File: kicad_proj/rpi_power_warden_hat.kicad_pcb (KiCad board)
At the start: 4 copper layers, 65 x 56.5 mm, 67 parts, among them J1 54-00164, J2 54-00164, J3 54-00003, J4 Raspberry Pi SMT connector, J5 Conn_01x02, Q1 DMG2305UX-7, Q2 DMG2305UX-7, U1 INA260, U10 SN74AHC1G08DBVR, U2 INA260, U3 CAT24C32WI-GT3, U4 TPS563200, U5 DMMT5401-7-F, U6 TPS563200, U7 DMMT5401-7-F, U8 TPS22810DBVR, U9 SN74AHC1G08DBVR

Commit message: progress with layout
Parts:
- moved C17 4.25 mm to (154.5, 82.9), turned to 0 degrees
- moved U10 1.32 mm to (154.1, 85.5)
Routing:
- added copper zone on F.Cu, net /current_sensor_5V/+VCC_OUT
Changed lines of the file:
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@@
 	(footprint "rpi_power_warden_hat:SOT-23-5"
 		(layer "F.Cu")
-		(at 153.5653 86.672448)
+		(at 154.088679 85.458721)
 		(descr "SOT, 5 Pin (JEDEC MO-178 Var AA https://www.jedec.org/document_search?search_api_views_fulltext=MO-178), generated with kicad-footprint-generator ipc_gullwing_generator.py")
 		(tags "SOT TO_SOT_SMD")
 		(property "Reference" "U10"
-			(at 0 -2.61 0)
+			(at 0 2.3368 0)
 			(layer "F.SilkS")
 			(effects
@@
 	(footprint "Capacitor_SMD:C_0603_1608Metric_Pad1.08x0.95mm_HandSolder"
 		(layer "F.Cu")
-		(at 156.561479 86.622448 90)
+		(at 154.459658 82.924194)
 		(descr "Capacitor SMD 0603 (1608 Metric), square (rectangular) end terminal, IPC_7351 nominal with elongated pad for handsoldering. (Body size source: IPC-SM-782 page 76, https://www.pcb-3d.com/wordpress/wp-content/uploads/ipc-sm-782a_amendment_1_and_2.pdf), generated with kicad-footprint-generator")
 		(tags "capacitor handsolder")
 		(property "Reference" "C17"
-			(at 0.011327 1.515 90)
+			(at 0.011327 -1.224673 360)
 			(layer "F.SilkS")
 			(effects
@@
 		)
 		(property "Value" "100 nF"
-			(at 0 1.43 90)
+			(at 0 1.43 360)
 			(layer "F.Fab")
 			(effects
@@
 		)
 		(property "Footprint" "Capacitor_SMD:C_0603_1608Metric_Pad1.08x0.95mm_HandSolder"
-			(at 0 0 90)
+			(at 0 0 0)
 			(unlocked yes)
 			(layer "F.Fab")
@@
 		)
 		(property "Datasheet" ""
-			(at 0 0 90)
+			(at 0 0 0)
 			(unlocked yes)
 			(layer "F.Fab")
@@
 		)
 		(property "Description" "CAP 0603 25V 100 NF X5R"
-			(at 0 0 90)
+			(at 0 0 0)
 			(unlocked yes)
 			(layer "F.Fab")
@@
 		)
 		(property "mpn" "CC0603KRX5R8BB104"
-			(at 0 0 90)
+			(at 0 0 0)
 			(unlocked yes)
 			(layer "F.Fab")
@@
 		)
 		(property "manufacturer" "YAGEO"
-			(at 0 0 90)
+			(at 0 0 0)
 			(unlocked yes)
 			(layer "F.Fab")
@@
 		)
 		(fp_line
-			(start 1.65 -0.73)
-			(end 1.65 0.73)
+			(start -1.65 -0.73)
+			(end 1.65 -0.73)
 			(stroke
 				(width 0.05)
@@
 		)
 		(fp_line
-			(start -1.65 -0.73)
-			(end 1.65 -0.73)
+			(start -1.65 0.73)
+			(end -1.65 -0.73)
 			(stroke
 				(width 0.05)
@@
 		)
 		(fp_line
-			(start 1.65 0.73)
-			(end -1.65 0.73)
+			(start 1.65 -0.73)
+			(end 1.65 0.73)
 			(stroke
 				(width 0.05)
@@
 		)
 		(fp_line
-			(start -1.65 0.73)
-			(end -1.65 -0.73)
+			(start 1.65 0.73)
+			(end -1.65 0.73)
 			(stroke
 				(width 0.05)
@@
 		)
 		(fp_line
-			(start 0.8 -0.4)
-			(end 0.8 0.4)
+			(start -0.8 -0.4)
+			(end 0.8 -0.4)
 			(stroke
 				(width 0.1)
@@
 		)
 		(fp_line
-			(start -0.8 -0.4)
-			(end 0.8 -0.4)
+			(start -0.8 0.4)
+			(end -0.8 -0.4)
 			(stroke
 				(width 0.1)
@@
 		)
 		(fp_line
-			(start 0.8 0.4)
-			(end -0.8 0.4)
+			(start 0.8 -0.4)
+			(end 0.8 0.4)
 			(stroke
 				(width 0.1)
@@
 		)
 		(fp_line
-			(start -0.8 0.4)
-			(end -0.8 -0.4)
+			(start 0.8 0.4)
+			(end -0.8 0.4)
 			(stroke
 				(width 0.1)
@@
 		)
 		(fp_text user "${REFERENCE}"
-			(at 0 0 90)
+			(at 0 0 360)
 			(layer "F.Fab")
 			(effects
@@
 		)
 		(pad "1" smd roundrect
-			(at -0.8625 0 90)
+			(at -0.8625 0)
 			(size 1.075 0.95)
 			(layers "F.Cu" "F.Paste" "F.Mask")
@@
 		)
 		(pad "2" smd roundrect
-			(at 0.8625 0 90)
+			(at 0.8625 0)
 			(size 1.075 0.95)
 			(layers "F.Cu" "F.Paste" "F.Mask")
@@
 	)
 	(gr_rect
-		(start 151.379479 83.335169)
+		(start 151.379479 80.957321)
 		(end 158.745479 88.501121)
 		(stroke
@@
 	)
 	(segment
-		(start 160.311059 105.8892)
-		(end 160.311059 104.0781)
-		(width 0.5)
+		(start 160.311059 104.0781)
+		(end 160.416759 103.9724)
+		(width 0.254)
 		(layer "F.Cu")
 		(net 3)
 	)
 	(segment
-		(start 160.311059 104.0781)
-		(end 160.416759 103.9724)
-		(width 0.254)
+		(start 160.641879 105.973071)
+		(end 160.641879 104.161971)
+		(width 0.5)
 		(layer "F.Cu")
 		(net 3)
@@
 	(segment
 		(start 168.973079 104.559521)
-		(end 169.074679 104.661121)
-		(width 0.254)
-		(layer "F.Cu")
-		(net 6)
-	)
-	(segment
-		(start 166.382279 104.559521)
-		(end 168.973079 104.559521)
+		(end 166.382279 104.559521)
 		(width 0.254)
 		(layer "F.Cu")
@@
 	)
 	(via
-		(at 169.074679 104.661121)
+		(at 168.973079 104.559521)
 		(size 0.45)
 		(drill 0.15)
@@
 	)
 	(segment
-		(start 169.074679 104.661121)
-		(end 169.074679 100.327321)
+		(start 168.973079 104.559521)
+		(end 168.973079 100.225721)
 		(width 0.254)
 		(layer "B.Cu")
@@
 	)
 	(segment
-		(start 169.074679 100.327321)
+		(start 168.973079 100.225721)
 		(end 164.299479 95.552121)
 		(width 0.254)
@@
 	)
 	(segment
-		(start 154.7028 87.622448)
-		(end 154.7028 88.4006)
-		(width 0.254)
-		(layer "F.Cu")
-		(net 71)
-	)
-	(segment
-		(start 154.7028 88.4006)
-		(end 154.698279 88.405121)
+		(start 155.226179 86.408721)
+		(end 155.226179 87.877221)
 		(width 0.254)
 		(layer "F.Cu")
@@
 	)
 	(via
-		(at 154.698279 88.455921)
+		(at 155.226179 87.877221)
 		(size 0.45)
 		(drill 0.15)
@@
 	)
 	(segment
-		(start 156.222279 88.455921)
-		(end 154.698279 88.455921)
+		(start 155.643579 87.877221)
+		(end 168.058679 100.292321)
 		(width 0.254)
 		(layer "B.Cu")
@@
 	(segment
 		(start 168.058679 100.292321)
-		(end 156.222279 88.455921)
+		(end 168.058679 102.933921)
 		(width 0.254)
 		(layer "B.Cu")
@@
 	)
 	(segment
-		(start 168.058679 102.933921)
-		(end 168.058679 100.292321)
+		(start 155.226179 87.877221)
+		(end 155.643579 87.877221)
 		(width 0.254)
 		(layer "B.Cu")
@@
 			(thermal_gap 0.25)
 			(thermal_bridge_width 0.5)
+			(smoothing chamfer)
+			(radius 0.15)
 		)
 		(polygon
 			(pts
 				(xy 160.489479 91.554721) (xy 160.489479 93.617824) (xy 153.674352 93.614854) (xy 153.680891 89.065521)
-				(xy 157.746279 89.065521) (xy 157.746279 90.945121) (xy 162.521479 90.945121) (xy 163.131079 91.554721)
+				(xy 156.641263 89.065521) (xy 156.621654 82.102972) (xy 163.334279 82.108235) (xy 163.334279 84.645921)
+				(xy 158.408358 84.645921) (xy 158.406679 89.064905) (xy 160.895879 89.065695) (xy 163.364726 91.554721)
 			)
 		)
@@
 			)
 		)
+	)
+	(zone
+		(net 15)
+		(net_name "/current_sensor_5V/+VCC_OUT")
+		(layer "F.Cu")
+		(hatch edge 0.5)
+		(priority 2)
+		(connect_pads
+			(clearance 0.25)
+		)
+		(min_thickness 0.25)
+		(filled_areas_thickness no)
+		(fill yes
+			(thermal_gap 0.25)
+			(thermal_bridge_width 0.5)
+			(smoothing chamfer)
+			(radius 0.15)
+		)
+		(polygon
+			(pts
+				(xy 165.772679 84.645921) (xy 172.173479 84.645921) (xy 172.173479 84.645921) (xy 172.173479 93.434321)
+				(xy 172.173479 93.434321) (xy 179.082279 93.434321) (xy 179.133079 93.383521) (xy 179.133079 90.843521)
+				(xy 179.082279 90.792721) (xy 174.662679 90.792721) (xy 174.662679 90.792721) (xy 174.662679 82.055121)
+				(xy 174.662679 82.055121) (xy 165.772679 82.055121)
+			)
+		)

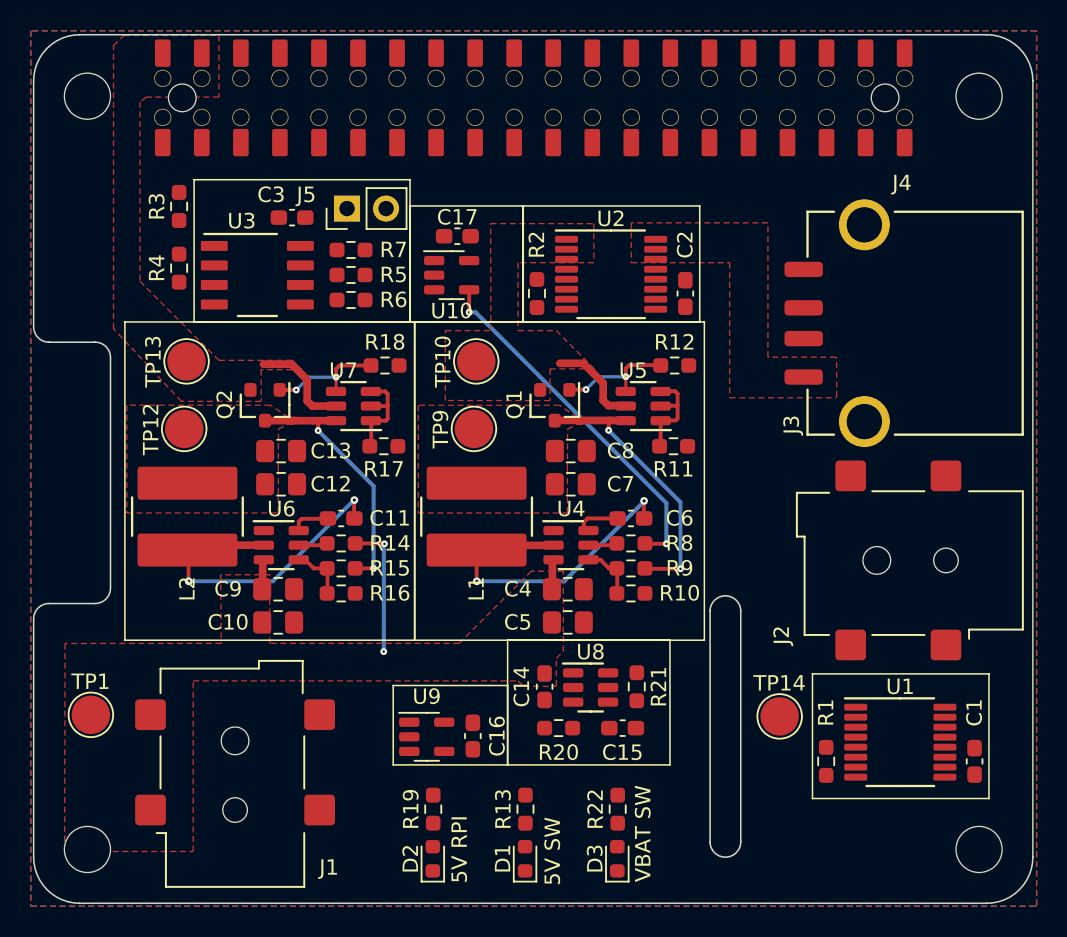
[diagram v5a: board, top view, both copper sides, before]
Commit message: feat: replace tht jumper by as solder bridge. feat: progress with layout.
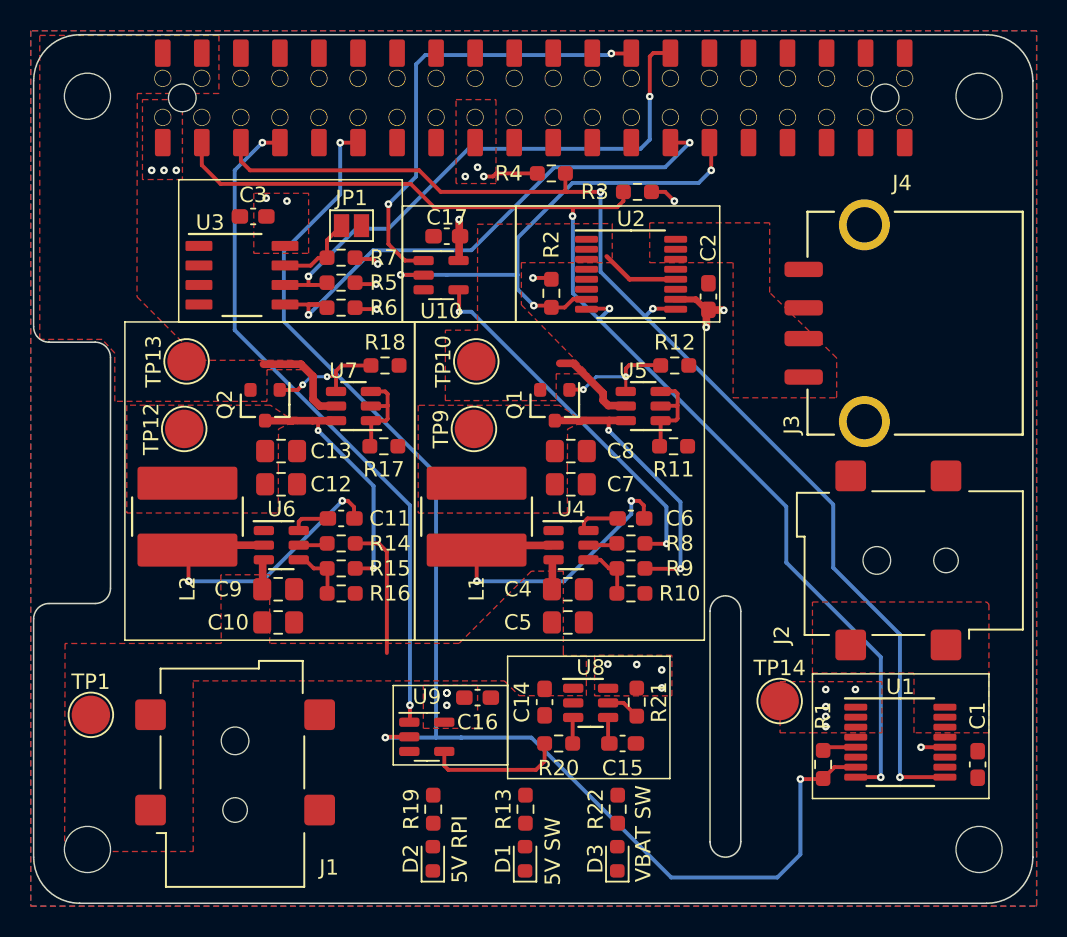
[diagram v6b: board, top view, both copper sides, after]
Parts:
- removed J5: Conn_01x02, Connector_PinHeader_2.54mm:PinHeader_1x02_P2.54mm_Vertical
- added JP1: SolderJumper_2_Open, Jumper:SolderJumper-2_P1.3mm_Open_Pad1.0x1.5mm, F.Cu at (147.6, 82.2)
- moved R3 29.8 mm to (166.2, 80.0), turned to 180 degrees
- moved R4 25.0 mm to (160.6, 78.8), turned to 0 degrees
- moved C3 2.54 mm to (141.2, 81.6)
- moved C16 2.52 mm to (155.8, 112.9), turned to 180 degrees
- moved C2 1.51 mm to (170.8, 86.8)
- moved U2 1.30 mm to (165.8, 85.4)
- moved C14 1.00 mm to (160.1, 113.2)
- moved C15 1.00 mm to (165.2, 115.9)
- moved R20 1.00 mm to (161.0, 115.9)
- moved R21 1.00 mm to (166.1, 113.2)
- moved TP14 1.00 mm to (175.4, 113.2)
- moved U3 1.00 mm to (140.4, 85.4)
- moved U8 1.00 mm to (163.1, 113.3)
- moved R2 0.94 mm to (160.6, 86.6), turned to 90 degrees
- moved R5 0.82 mm to (146.9, 85.9)
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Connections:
- J4 pad 26: /rpi/ENA_VBAT_SW -> /rpi/ENA_5V_SW
- J4 pad 29: /rpi/ENA_5V_SW -> /rpi/INA_5V_ALERT
- J4 pad 7: /rpi/INA_5V_ALERT -> /rpi/ENA_VBAT_SW
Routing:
- net /rpi/INA_VBAT_ALERT: track 0.00 -> 87.3 mm, vias 0 -> 3
- net /INA_SDA: track 0.00 -> 80.3 mm, vias 0 -> 3
- net /INA_SCL: track 0.00 -> 77.6 mm, vias 0 -> 3
- net /rpi/ENA_VBAT_SW: track 0.00 -> 44.3 mm, vias 0 -> 2
- net /rpi/ID_SC_I2C0: track 0.00 -> 36.4 mm, vias 0 -> 2
- net /rpi/ID_SD_I2C0: track 0.00 -> 34.9 mm, vias 0 -> 2
- net /rpi/INA_5V_ALERT: track 0.00 -> 33.6 mm, vias 0 -> 3
- net /rpi/ENA_5V_SW: track 0.00 -> 29.5 mm, vias 0 -> 2
- net /+3V3: track 0.00 -> 20.0 mm, vias 0 -> 19
- net /and_vbat/Y: track 0.00 -> 8.96 mm
- net Net-(JP1-B): track 0.00 -> 5.49 mm
- net /current_sensor_5V/+VCC_IN: track 6.19 -> 10.9 mm
- net Net-(U8-QOD): track 0.00 -> 2.22 mm
- net Net-(U8-CT): track 0.00 -> 1.73 mm
- net Net-(U8-EN/UVLO): track 0.00 -> 1.71 mm
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- added copper zone on F.Cu, net /+3V3
- added copper zone on In2.Cu, net /+3V3
- added copper zone on F.Cu, net /current_sensor_VBAT/+VCC_IN
- added copper zone on In2.Cu, net /current_sensor_VBAT/+VCC_IN
- added copper zone on F.Cu, net /current_sensor_VBAT/+VCC_OUT

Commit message: fix: all DRCs in PCB. First layout is done.
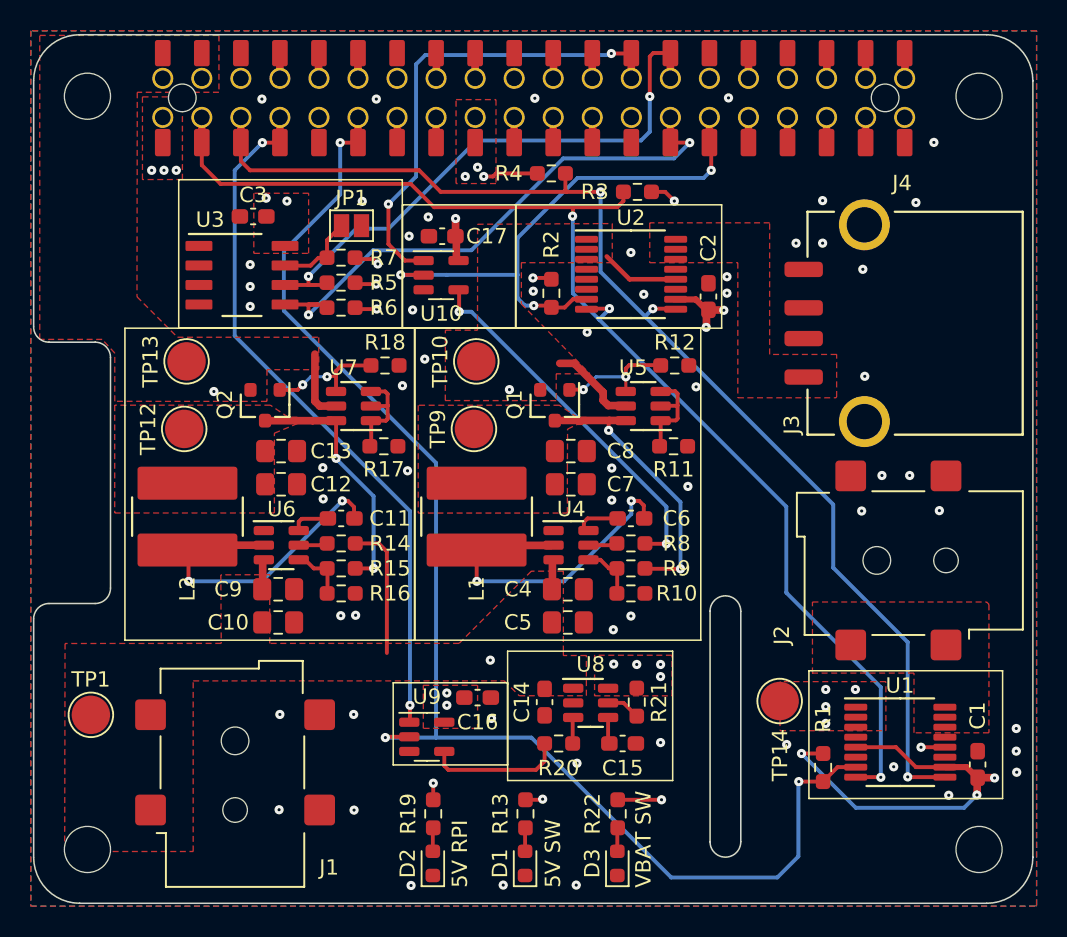
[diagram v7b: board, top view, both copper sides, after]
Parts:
- moved D1 0.30 mm to (158.9, 123.7)
- moved D2 0.30 mm to (152.9, 123.7)
- moved D3 0.30 mm to (164.9, 123.7)
- moved R13 0.30 mm to (158.9, 120.5)
- moved R19 0.30 mm to (152.9, 120.5)
- moved R22 0.30 mm to (164.9, 120.5)
- moved C17 0.30 mm to (153.5, 82.9)
- moved R1 0.20 mm to (178.3, 117.5)
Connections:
- net /rpi/CE0_SPI0/GPIO08_1 renamed /rpi/CE0_SPI0/GPIO08
- net /rpi/GPCLK2/GPIO06_1 renamed /rpi/GPCLK2/GPIO06
- net /rpi/GPIO12/PWM0 renamed /rpi/GPIO12/PWM0_1
- net /rpi/GPIO13/PWM1_1 renamed /rpi/GPIO13/PWM1
- net /rpi/GPIO14/UART_TXD renamed /rpi/GPIO14/UART_TXD_1
- net /rpi/GPIO15/UART_RXD renamed /rpi/GPIO15/UART_RXD_1
- net /rpi/GPIO16/SP1_CE2 renamed /rpi/GPIO16/SP1_CE2_1
- net /rpi/GPIO18/SPI1_CE0_1 renamed /rpi/GPIO18/SPI1_CE0
- net /rpi/GPIO19/SPI1_MISO renamed /rpi/GPIO19/SPI1_MISO_1
- net /rpi/GPIO20/SPI1_MOSI renamed /rpi/GPIO20/SPI1_MOSI_1
- net /rpi/GPIO21/SPI1_CLK_1 renamed /rpi/GPIO21/SPI1_CLK
- net /rpi/GPIO22/SDIO_CLK renamed /rpi/GPIO22/SDIO_CLK_1
- net /rpi/GPIO23/SDIO_CMD_1 renamed /rpi/GPIO23/SDIO_CMD
- net /rpi/GPIO24/SDIO_DAT0_1 renamed /rpi/GPIO24/SDIO_DAT0
- net /rpi/GPIO25/SDIO_DAT1 renamed /rpi/GPIO25/SDIO_DAT1_1
- net /rpi/GPIO26/SDIO_DAT2 renamed /rpi/GPIO26/SDIO_DAT2_1
- net /rpi/GPIO27/SDIO_DAT3_1 renamed /rpi/GPIO27/SDIO_DAT3
- net /rpi/MISO_SPI0/GPIO09 renamed /rpi/MISO_SPI0/GPIO09_1
- net /rpi/MOSI_SPI0/GPIO10 renamed /rpi/MOSI_SPI0/GPIO10_1
- net /rpi/SCLK_SPI0/GPIO11 renamed /rpi/SCLK_SPI0/GPIO11_1
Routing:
- net /rpi/+5V_RPI: track 6.43 -> 36.7 mm, vias 0 -> 2
- net /current_sensor_5V/+VCC_IN: track 10.9 -> 39.7 mm, vias 0 -> 2
- net /+3V3: track 20.0 -> 43.8 mm, vias 19 -> 21
- net /current_sensor_VBAT/+VCC_IN: track 1.58 -> 4.43 mm
- net /rpi/INA_5V_ALERT: track 33.6 -> 35.6 mm
- net /rpi/SCLK_SPI0/GPIO11_1: track 0.00 -> 1.64 mm
- net /rpi/MOSI_SPI0/GPIO10_1: track 0.00 -> 1.64 mm
- net /rpi/MISO_SPI0/GPIO09_1: track 0.00 -> 1.64 mm
- net /rpi/ID_SD_I2C0: track 34.9 -> 36.6 mm
- net /rpi/GPIO27/SDIO_DAT3: track 0.00 -> 1.64 mm
- net /rpi/GPIO26/SDIO_DAT2_1: track 0.00 -> 1.64 mm
- net /rpi/GPIO25/SDIO_DAT1_1: track 0.00 -> 1.64 mm
- net /rpi/GPIO24/SDIO_DAT0: track 0.00 -> 1.64 mm
- net /rpi/GPIO23/SDIO_CMD: track 0.00 -> 1.64 mm
- net /rpi/GPIO22/SDIO_CLK_1: track 0.00 -> 1.64 mm
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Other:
- rule pad_to_mask_clearance: 0 -> 0.038

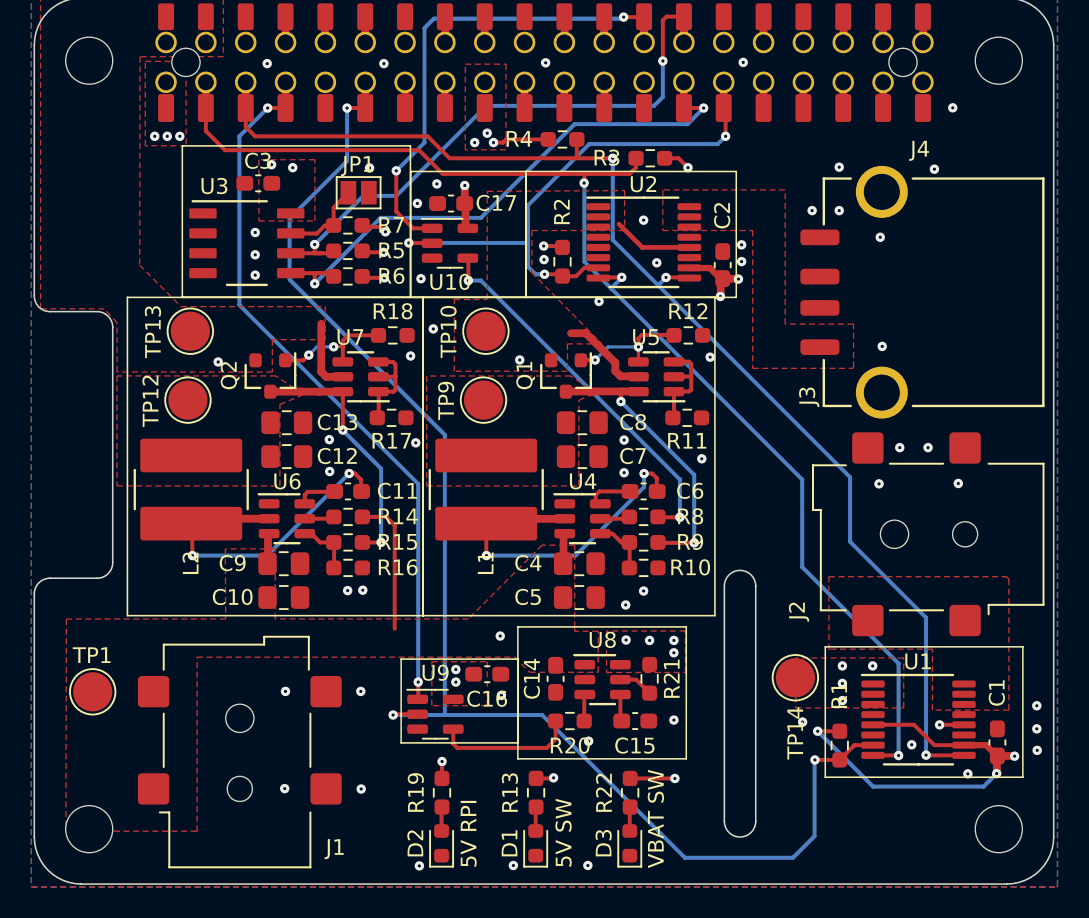
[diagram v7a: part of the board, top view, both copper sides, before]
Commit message: add powa logo image
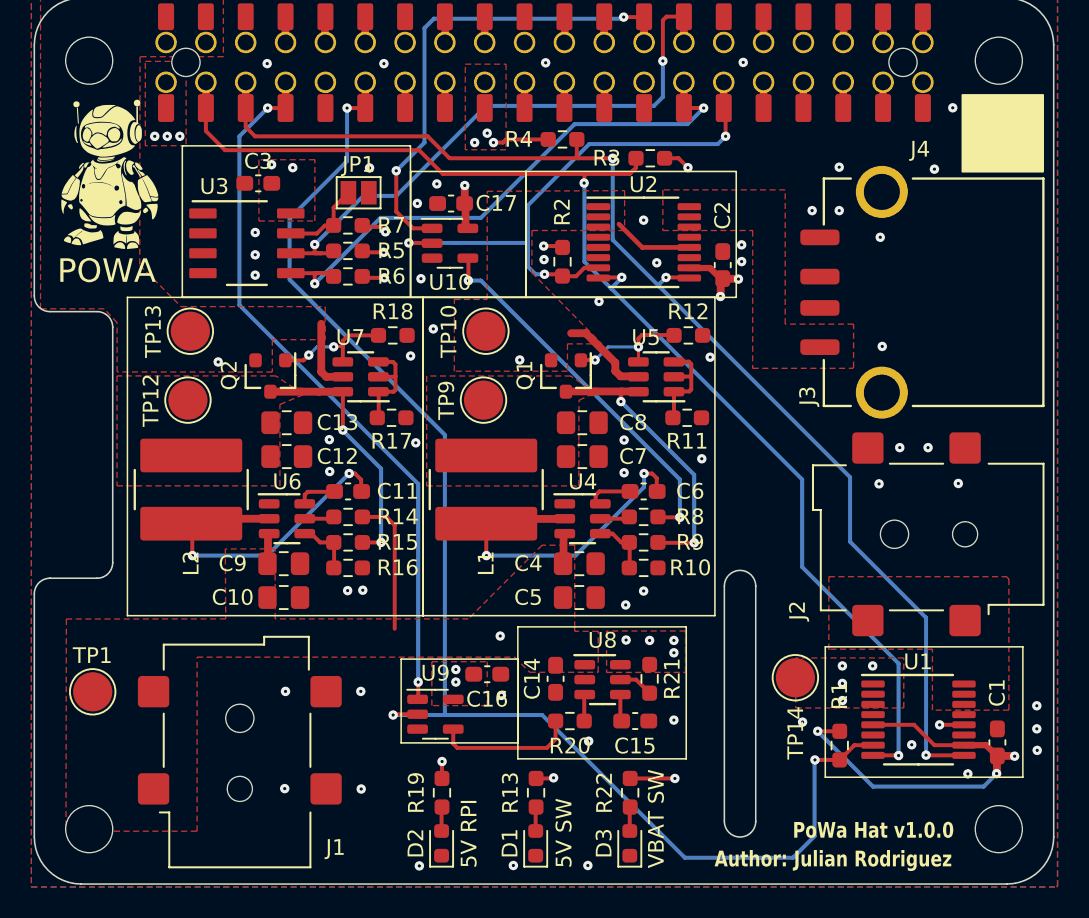
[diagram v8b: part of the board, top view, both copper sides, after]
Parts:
- added G***: POWA, rpi_power_warden_hat:powa_logo, F.Cu at (131.5, 81.0)
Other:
- board text added: "Author: Julian Rodriguez"
- board text added: "PoWa Hat v1.0.0"
